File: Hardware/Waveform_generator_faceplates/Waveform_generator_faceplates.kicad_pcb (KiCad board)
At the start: 2 copper layers, 88 x 78 mm, 12 parts

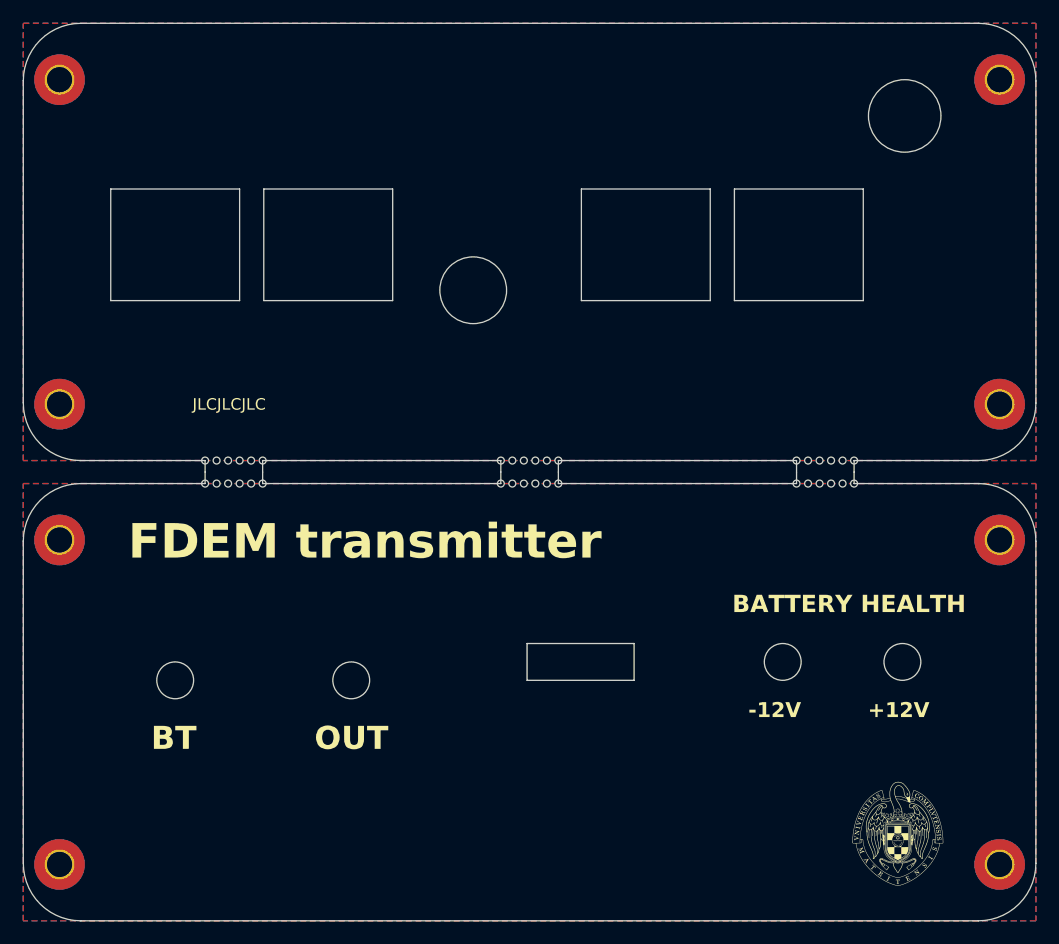
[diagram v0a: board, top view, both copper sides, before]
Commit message: Revisión 1 del hardware. Reorganizaco un poco el layout y añadidos shottky de protección, puente para desconectar el buck, conectores de pogo para conectar a masa la carcasa de aluminio, agrandado el espacio del powerOpAmp para un mayor disipador...
Actualizado el controlador para que por USB no printee la batería todo el rato.

Añadida opción de reseteo del AD9837 en cada comando para probar si se soluciona el problema  (no genera nada a la salida)
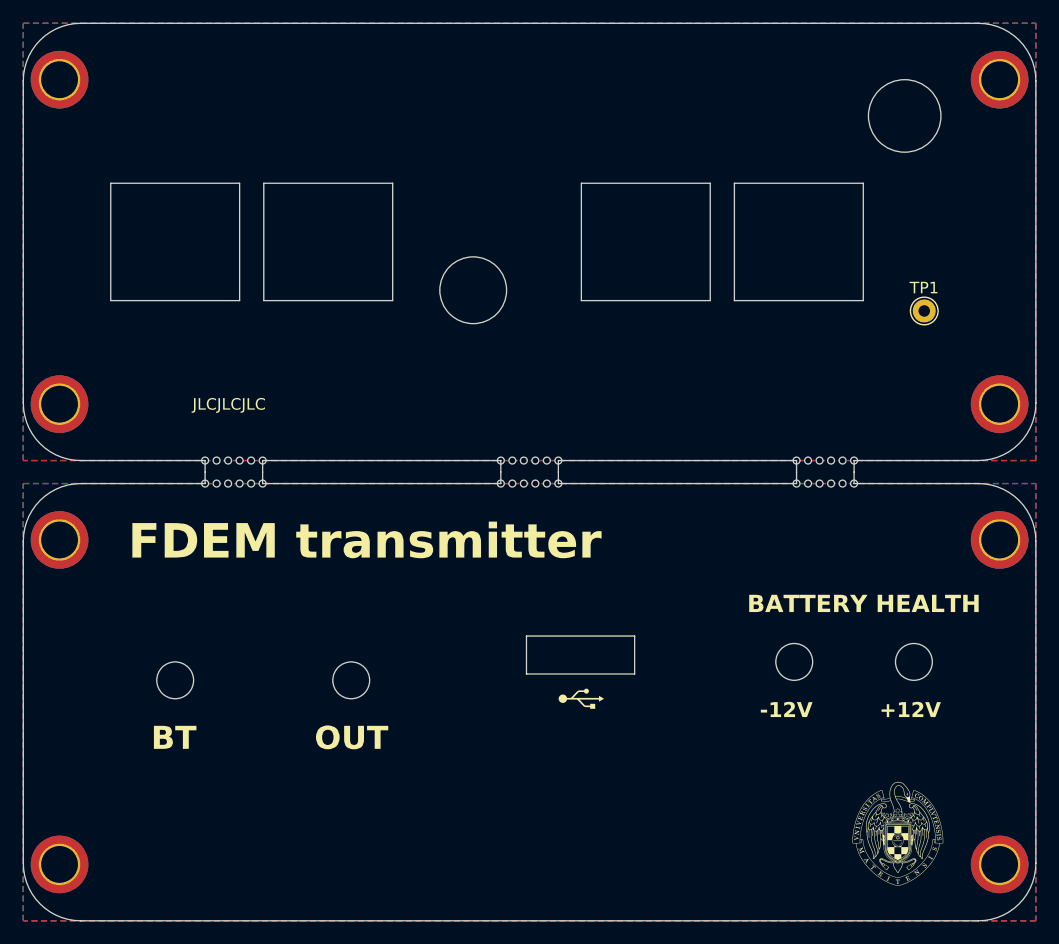
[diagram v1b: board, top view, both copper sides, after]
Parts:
- added G***: LOGO, customfootprints.preety:USB_2_0, F.Cu at (96.5, 114.7)
- added TP1: TP, TestPoint:TestPoint_THTPad_D2.0mm_Drill1.0mm, F.Cu at (126.3, 81.0)
- H1, H2, H3, H4, H5, H6, H7, H8: footprint MountingHole:MountingHole_2.2mm_M2_Pad_TopBottom -> CUSTOM:M3 hole (3.2mm hole Pad 5mm)
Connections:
- H5 pad 1: GND -> GND1
- H6 pad 1: GND -> GND1
- H7 pad 1: GND -> GND1
- H8 pad 1: GND -> GND1
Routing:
- added copper zone on B.Cu, net GND1
- added copper zone on F.Cu, net GND1
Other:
- outline, holes or cut-outs redrawn

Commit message: Rev 2 de hardware actualizada con error en los pines del ad9837 (SCLK y CS intercambiados). ERROR IDENTIFICADO
Añadida corrección del offset que hay a la salida del ad9837 que antes no se tenía en cuenta.
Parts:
- added G***: LOGO, customfootprints.preety:Bluetooth_fill, F.Cu at (61.2, 118.0)
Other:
- board text removed: "BT"
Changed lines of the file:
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@@
 		(embedded_fonts no)
 	)
+	(footprint "customfootprints.preety:Bluetooth_fill"
+		(layer "F.Cu")
+		(at 61.2 118)
+		(property "Reference" "G***"
+			(at 0 0 0)
+			(layer "F.SilkS")
+			(hide yes)
+			(effects
+				(font
+					(size 1.5 1.5)
+					(thickness 0.3)
+				)
+			)
+		)
+		(property "Value" "LOGO"
+			(at 0.158202 0 0)
+			(layer "F.SilkS")
+			(hide yes)
+			(effects
+				(font
+					(size 1.5 1.5)
+					(thickness 0.3)
+				)
+			)
+		)
+		(property "Datasheet" ""
+			(at 0 0 0)
+			(layer "F.Fab")
+			(hide yes)
+			(effects
+				(font
+					(size 1.27 1.27)
+				)
+			)
+		)
+		(property "Description" ""
+			(at 0 0 0)
+			(layer "F.Fab")
+			(hide yes)
+			(effects
+				(font
+					(size 1.27 1.27)
+				)
+			)
+		)
+		(attr board_only exclude_from_pos_files exclude_from_bom)
+		(duplicate_pad_numbers_are_jumpers no)
+		(fp_poly
+			(pts
+				(xy 0.180728 -1.114716) (xy 0.19132 -1.104822) (xy 0.207611 -1.089164) (xy 0.228903 -1.068423) (xy 0.254502 -1.043282)
+				(xy 0.28371 -1.01442) (xy 0.315833 -0.982521) (xy 0.350174 -0.948264) (xy 0.354955 -0.943483) (xy 0.529584 -0.7688)
+				(xy 0.351159 -0.590427) (xy 0.172732 -0.412053) (xy 0.172732 -0.76511) (xy 0.172785 -0.82368) (xy 0.172937 -0.879214)
+				(xy 0.17318 -0.930908) (xy 0.173505 -0.97796) (xy 0.173904 -1.019566) (xy 0.174367 -1.054924) (xy 0.174888 -1.083231)
+				(xy 0.175455 -1.103685) (xy 0.176061 -1.115482) (xy 0.176529 -1.118166)
+			)
+			(stroke
+				(width 0)
+				(type solid)
+			)
+			(fill yes)
+			(layer "F.SilkS")
+		)
+		(fp_poly
+			(pts
+				(xy 0.180926 0.342849) (xy 0.191518 0.35264) (xy 0.207469 0.367932) (xy 0.227943 0.387884) (xy 0.252099 0.411654)
+				(xy 0.279103 0.438403) (xy 0.308117 0.46729) (xy 0.338302 0.497475) (xy 0.368822 0.528115) (xy 0.39884 0.558372)
+				(xy 0.427518 0.587405) (xy 0.454017 0.614373) (xy 0.477502 0.638434) (xy 0.497135 0.658749) (xy 0.512079 0.674478)
+				(xy 0.521496 0.684779) (xy 0.524559 0.688765) (xy 0.521106 0.693207) (xy 0.511202 0.704034) (xy 0.495525 0.720548)
+				(xy 0.474756 0.742049) (xy 0.449573 0.767838) (xy 0.420657 0.797217) (xy 0.388689 0.829488) (xy 0.354345 0.86395)
+				(xy 0.348645 0.869651) (xy 0.172732 1.04551) (xy 0.172732 0.692454) (xy 0.172785 0.633884) (xy 0.172937 0.578351)
+				(xy 0.17318 0.526656) (xy 0.173505 0.479605) (xy 0.173904 0.437998) (xy 0.174368 0.40264) (xy 0.174888 0.374332)
+				(xy 0.175455 0.35388) (xy 0.176061 0.342083) (xy 0.176529 0.339399)
+			)
+			(stroke
+				(width 0)
+				(type solid)
+			)
+			(fill yes)
+			(layer "F.SilkS")
+		)
+		(fp_poly
+			(pts
+				(xy 0.081492 -2.176942) (xy 0.214242 -2.169801) (xy 0.33993 -2.155659) (xy 0.4587 -2.134442) (xy 0.570699 -2.106074)
+				(xy 0.676071 -2.070482) (xy 0.774963 -2.027591) (xy 0.867519 -1.977326) (xy 0.953886 -1.919614)
+				(xy 1.03421 -1.85438) (xy 1.108635 -1.78155) (xy 1.177308 -1.701048) (xy 1.240374 -1.612802) (xy 1.29798 -1.516736)
+				(xy 1.321361 -1.472505) (xy 1.370387 -1.367073) (xy 1.414229 -1.253665) (xy 1.452901 -1.132202)
+				(xy 1.486416 -1.002606) (xy 1.51479 -0.864796) (xy 1.538037 -0.718698) (xy 1.556169 -0.56423) (xy 1.569201 -0.401315)
+				(xy 1.57715 -0.229874) (xy 1.580026 -0.049829) (xy 1.580037 -0.03721) (xy 1.577529 0.140725) (xy 1.570017 0.310751)
+				(xy 1.557517 0.472756) (xy 1.540046 0.62663) (xy 1.517622 0.772263) (xy 1.49026 0.909543) (xy 1.45798 1.038361)
+				(xy 1.420798 1.158606) (xy 1.37873 1.270168) (xy 1.378482 1.270761) (xy 1.328044 1.381524) (xy 1.272205 1.483962)
+				(xy 1.210828 1.578174) (xy 1.143774 1.664256) (xy 1.070908 1.742308) (xy 0.99209 1.812426) (xy 0.907184 1.874709)
+				(xy 0.816052 1.929255) (xy 0.718555 1.97616) (xy 0.614558 2.015523) (xy 0.503922 2.047441) (xy 0.386509 2.072012)
+				(xy 0.262182 2.089334) (xy 0.22048 2.0934) (xy 0.185237 2.095884) (xy 0.142485 2.097927) (xy 0.09463 2.099494)
+				(xy 0.044075 2.100553) (xy -0.006777 2.101069) (xy -0.055521 2.10101) (xy -0.099756 2.100341) (xy -0.137074 2.09903)
+				(xy -0.146423 2.098514) (xy -0.275885 2.086881) (xy -0.398757 2.06823) (xy -0.514908 2.0426) (xy -0.624206 2.010036)
+				(xy -0.726521 1.97058) (xy -0.821721 1.924274) (xy -0.909675 1.871161) (xy -0.961356 1.834186) (xy -1.04001 1.768354)
+				(xy -1.113096 1.695122) (xy -1.180659 1.614377) (xy -1.242749 1.526006) (xy -1.299411 1.429896)
+				(xy -1.350695 1.325937) (xy -1.396647 1.214014) (xy -1.437316 1.094016) (xy -1.472748 0.96583) (xy -1.502994 0.829343)
+				(xy -1.520383 0.728976) (xy -0.968219 0.728976) (xy -0.857616 0.839493) (xy -0.747013 0.95001) (xy -0.444189 0.647217)
+				(xy -0.398403 0.601479) (xy -0.354632 0.557837) (xy -0.313401 0.516811) (xy -0.275233 0.478915)
+				(xy -0.24065 0.444668) (xy -0.210175 0.414585) (xy -0.184332 0.389182) (xy -0.163644 0.368977) (xy -0.148632 0.354486)
+				(xy -0.139821 0.346225) (xy -0.137612 0.344424) (xy -0.137175 0.349357) (xy -0.136752 0.363783)
+				(xy -0.136347 0.387142) (xy -0.135962 0.418875) (xy -0.1356 0.458424) (xy -0.135264 0.505228) (xy -0.134957 0.558729)
+				(xy -0.134682 0.618367) (xy -0.134441 0.683583) (xy -0.134237 0.753817) (xy -0.134075 0.82851) (xy -0.133956 0.907104)
+				(xy -0.133881 0.989037) (xy -0.133857 1.071942) (xy -0.133857 1.79946) (xy 0.419008 1.24661) (xy 0.971877 0.693759)
+				(xy 0.607487 0.329343) (xy 0.557214 0.279021) (xy 0.508995 0.230661) (xy 0.463299 0.184741) (xy 0.420598 0.141739)
+				(xy 0.381362 0.102132) (xy 0.346063 0.066397) (xy 0.315171 0.035012) (xy 0.289158 0.008454) (xy 0.268495 -0.012799)
+				(xy 0.253652 -0.028272) (xy 0.2451 -0.037484) (xy 0.243098 -0.040002) (xy 0.246577 -0.044166) (xy 0.256702 -0.054949)
+				(xy 0.272997 -0.071871) (xy 0.29499 -0.094452) (xy 0.322206 -0.122211) (xy 0.354174 -0.154668) (xy 0.390421 -0.191344)
+				(xy 0.430472 -0.231759) (xy 0.473853 -0.275433) (xy 0.520092 -0.321885) (xy 0.568716 -0.370637)
+				(xy 0.60372 -0.405675) (xy 0.653736 -0.455733) (xy 0.701721 -0.503803) (xy 0.7472 -0.549409) (xy 0.789696 -0.59207)
+				(xy 0.828735 -0.63131) (xy 0.863843 -0.666648) (xy 0.894544 -0.697609) (xy 0.920363 -0.723712) (xy 0.940826 -0.74448)
+				(xy 0.955456 -0.759433) (xy 0.96378 -0.768094) (xy 0.965601 -0.770154) (xy 0.96225 -0.774067) (xy 0.952166 -0.784695)
+				(xy 0.935731 -0.801654) (xy 0.913326 -0.824557) (xy 0.885332 -0.85302) (xy 0.852132 -0.886657) (xy 0.814107 -0.925085)
+				(xy 0.77164 -0.967916) (xy 0.725112 -1.014765) (xy 0.674904 -1.065248) (xy 0.621399 -1.118979) (xy 0.564979 -1.175574)
+				(xy 0.506024 -1.234646) (xy 0.444917 -1.295811) (xy 0.416499 -1.324233) (xy -0.133857 -1.874576)
+				(xy -0.133857 -1.147057) (xy -0.133884 -1.062396) (xy -0.13396 -0.980526) (xy -0.134084 -0.902009)
+				(xy -0.134253 -0.827404) (xy -0.134463 -0.75727) (xy -0.134712 -0.692166) (xy -0.134997 -0.632652)
+				(xy -0.135313 -0.579287) (xy -0.13566 -0.532629) (xy -0.136032 -0.49324) (xy -0.13643 -0.461677)
+				(xy -0.136848 -0.4385) (xy -0.137283 -0.424269) (xy -0.137724 -0.419539) (xy -0.14178 -0.423013)
+				(xy -0.152407 -0.433091) (xy -0.16908 -0.449255) (xy -0.191275 -0.470985) (xy -0.218469 -0.497765)
+				(xy -0.250134 -0.529076) (xy -0.285751 -0.564401) (xy -0.324793 -0.603221) (xy -0.366736 -0.645018)
+				(xy -0.411057 -0.689275) (xy -0.442878 -0.721105) (xy -0.488515 -0.766752) (xy -0.532114 -0.8103)
+				(xy -0.573154 -0.851232) (xy -0.611113 -0.889027) (xy -0.645468 -0.92317) (xy -0.675697 -0.953144)
+				(xy -0.70128 -0.978429) (xy -0.721693 -0.998508) (xy -0.736416 -1.012865) (xy -0.744925 -1.02098)
+				(xy -0.746904 -1.02267) (xy -0.751005 -1.01925) (xy -0.761301 -1.009566) (xy -0.776903 -0.994491)
+				(xy -0.796918 -0.974889) (xy -0.820459 -0.95163) (xy -0.846634 -0.925585) (xy -0.85722 -0.915005)
+				(xy -0.964797 -0.807339) (xy -0.905667 -0.744366) (xy -0.886104 -0.723639) (xy -0.868887 -0.705606)
+				(xy -0.855206 -0.691493) (xy -0.846246 -0.682527) (xy -0.843281 -0.679888) (xy -0.839334 -0.676182)
+				(xy -0.828807 -0.665853) (xy -0.812209 -0.649407) (xy -0.790044 -0.627351) (xy -0.762819 -0.600192)
+				(xy -0.731043 -0.568434) (xy -0.69522 -0.532586) (xy -0.655858 -0.493154) (xy -0.613464 -0.450643)
+				(xy -0.568545 -0.405561) (xy -0.521607 -0.358413) (xy -0.521022 -0.357826) (xy -0.202021 -0.037271)
+				(xy -0.58512 0.345852) (xy -0.968219 0.728976) (xy -1.520383 0.728976) (xy -1.528098 0.684443) (xy -1.548109 0.531018)
+				(xy -1.558566 0.424842) (xy -1.564143 0.349557) (xy -1.568623 0.266409) (xy -1.571994 0.177393)
+				(xy -1.574243 0.08451) (xy -1.575357 -0.010243) (xy -1.575326 -0.104864) (xy -1.574136 -0.19736)
+				(xy -1.571775 -0.285729) (xy -1.568232 -0.367974) (xy -1.563869 -0.437131) (xy -1.549842 -0.592096)
+				(xy -1.531605 -0.738255) (xy -1.509051 -0.875976) (xy -1.482079 -1.005624) (xy -1.450586 -1.127568)
+				(xy -1.414466 -1.242175) (xy -1.373616 -1.349815) (xy -1.327935 -1.450853) (xy -1.277318 -1.545658)
+				(xy -1.230282 -1.621693) (xy -1.166055 -1.710081) (xy -1.095059 -1.791183) (xy -1.017578 -1.864752)
+				(xy -0.933896 -1.930548) (xy -0.844299 -1.988326) (xy -0.74907 -2.037841) (xy -0.740144 -2.041924)
+				(xy -0.652803 -2.07783) (xy -0.562029 -2.107922) (xy -0.466873 -2.132387) (xy -0.366384 -2.151414)
+				(xy -0.259614 -2.165191) (xy -0.145611 -2.173907) (xy -0.058466 -2.177155)
+			)
+			(stroke
+				(width 0)
+				(type solid)
+			)
+			(fill yes)
+			(layer "F.SilkS")
+		)
+		(embedded_fonts no)
+	)
 	(footprint "CUSTOM:Mouse-bite"
 		(layer "F.Cu")
@@
 				(bold yes)
 			)
-			(justify left bottom)
-		)
-	)
-	(gr_text "BT"
-		(at 59.1 119.3 0)
-		(layer "F.SilkS")
-		(effects
-			(font
-				(size 2 2)
-				(thickness 0.4)
-				(bold yes)
-			)
